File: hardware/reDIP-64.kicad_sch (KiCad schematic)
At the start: 0 parts

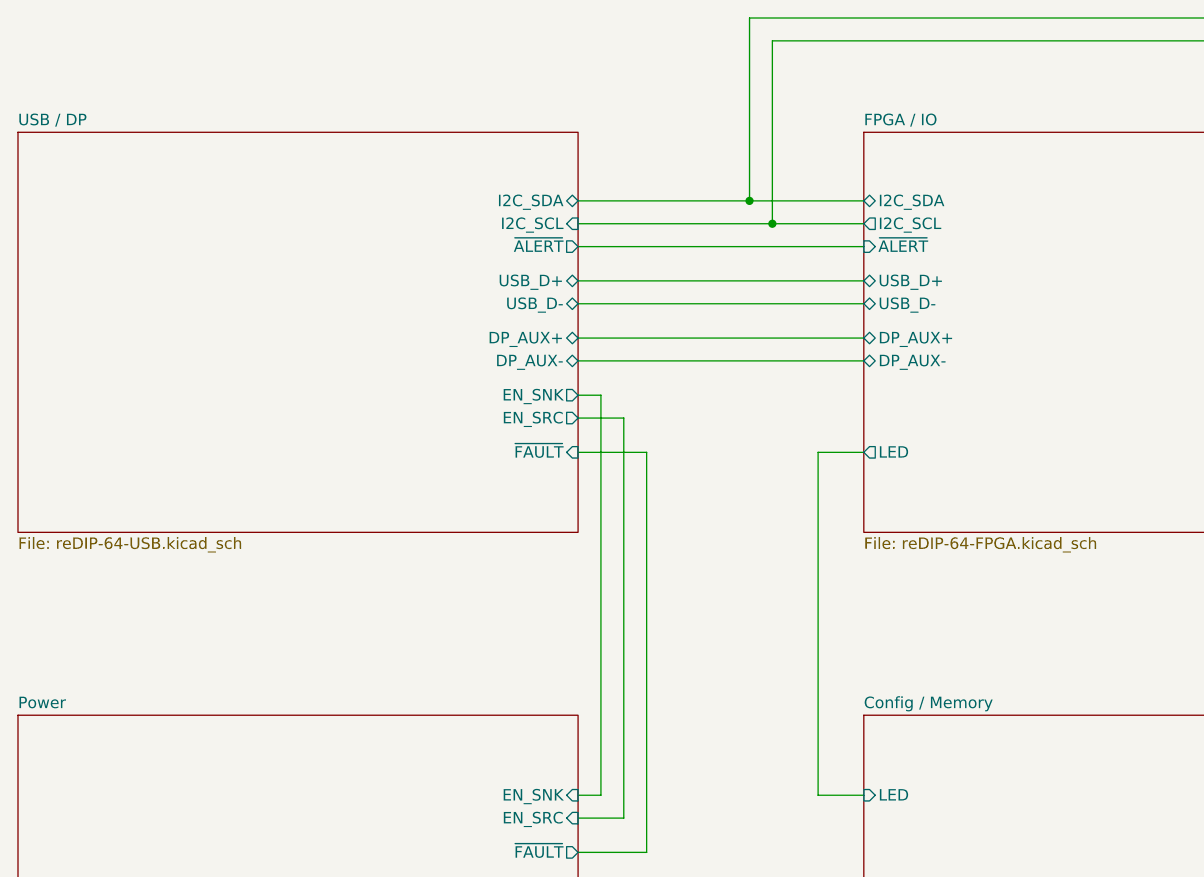
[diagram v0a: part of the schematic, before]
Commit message: Various improvements
* Removed slash from sheet names
* Reannotated schematics
* Example derivation of clocks in schematics
* Identical capacitors for DisplayPort main lanes and AUX
* Replaced switch FSA2259UMX with FSUSB42UMX
* Modified PCB physical stackup to (hopefully) be manufacturable
* Only one microvia size (0.1mm)
* Changed track width for differential pairs
* Routing cleanups and improvements
* Added files for manufacture
* Updated README

Many thanks for advice and help go to @azonenberg, @DX-MON, @gatecat,
@smunaut, and @zyp.
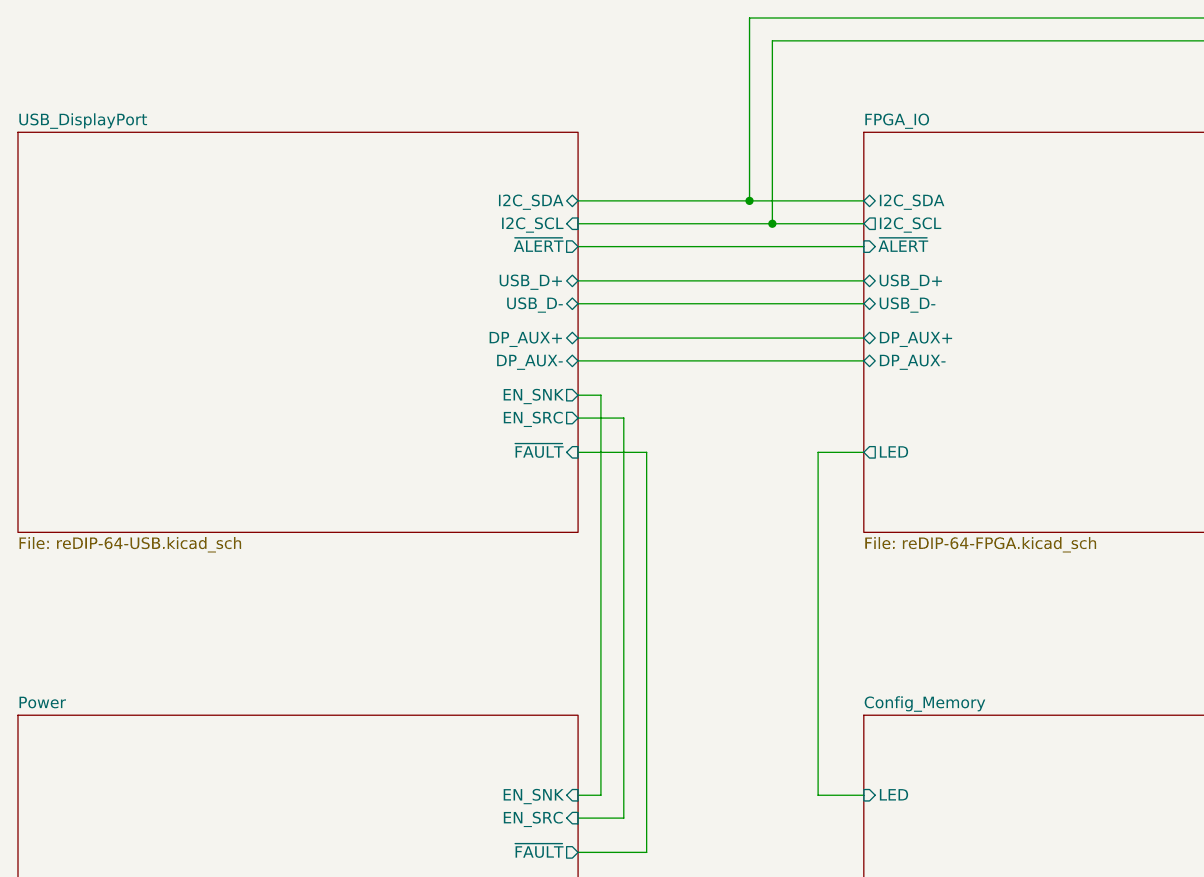
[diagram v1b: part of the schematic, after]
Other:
- sheet Config / Memory renamed Config_Memory
- sheet FPGA / IO renamed FPGA_IO
- sheet USB / DP renamed USB_DisplayPort

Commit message: Updated all KiCad files to current format
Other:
- sheet FPGA_IO ports: added ~{ALERT}; removed ~ALERT~
- sheet Power ports: added ~{FAULT}; removed ~FAULT~
- sheet USB_DisplayPort ports: added ~{ALERT}, ~{FAULT}; removed ~ALERT~, ~FAULT~

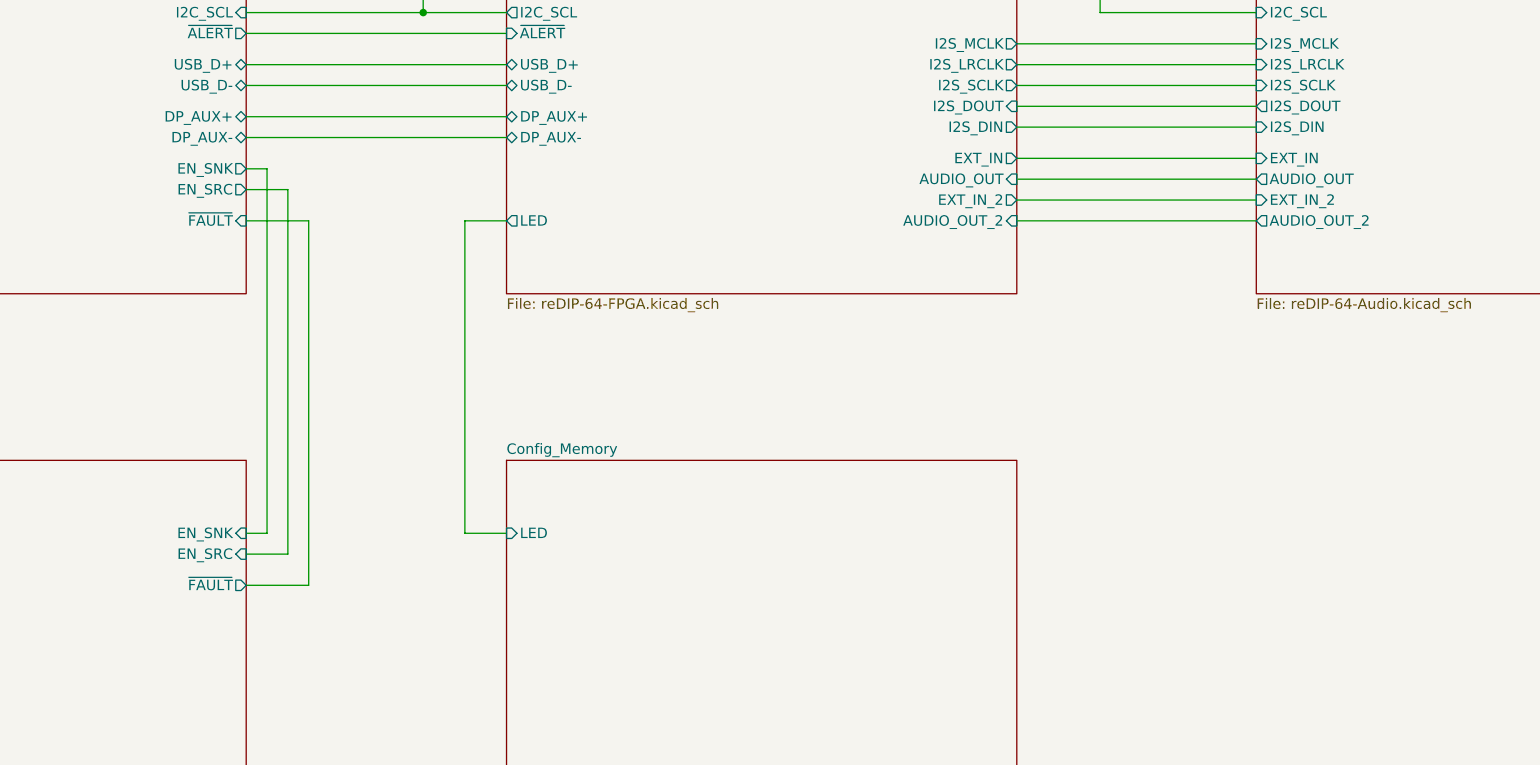
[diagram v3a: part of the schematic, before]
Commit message: Revision 1.0
* USB receptacle replaced with GCT USB4080-03-A / HRO TYPE-C-31-M-05
* USB PD TCPC changed to PTN5110NHQ (FPF2286 has 15ms VBUS debounce time)
* Complete rework of power section
  - Over-voltage protection on VBUS (FPF2286 / FPF2495C)
  - Bidirectional VCC (2 x TPS22916)
  - Replaced EOLed buck converters with FAN53610 / FAN53611
  - Replaced EOLed LDO for ECP5 VCCAUX with NCP115AMX250TCG
  - Replaced LDO for SGTL5000 VDDA with 3.3V version
  - Added separate LDO for SGTL5000 VDDD, avoiding overvoltage on ECP5 VCC
* Bus switch changed to SN74CBT16211A, biased for level shifting
* Registered I/O for FLASH / HyperRAM clock
* Pin header changes:
  - Machined (round) pins for MOS6510 socket
  - Top only headers for additional I/O
  - Reworked pinout for VIC-II and SID
  - Removed 5V output (now available on bidirectional VCC)
  - Added GND for audio / 3.3V
  - Changed JTAG pinout to match Tag-Connect TC-LATTICE / TC-XILINX6
* Removed EXT_IN capacitors
* Button force changed from 240gf to 100gf
* Space for UL and date codes
* Black solder mask
* Silk screen updates
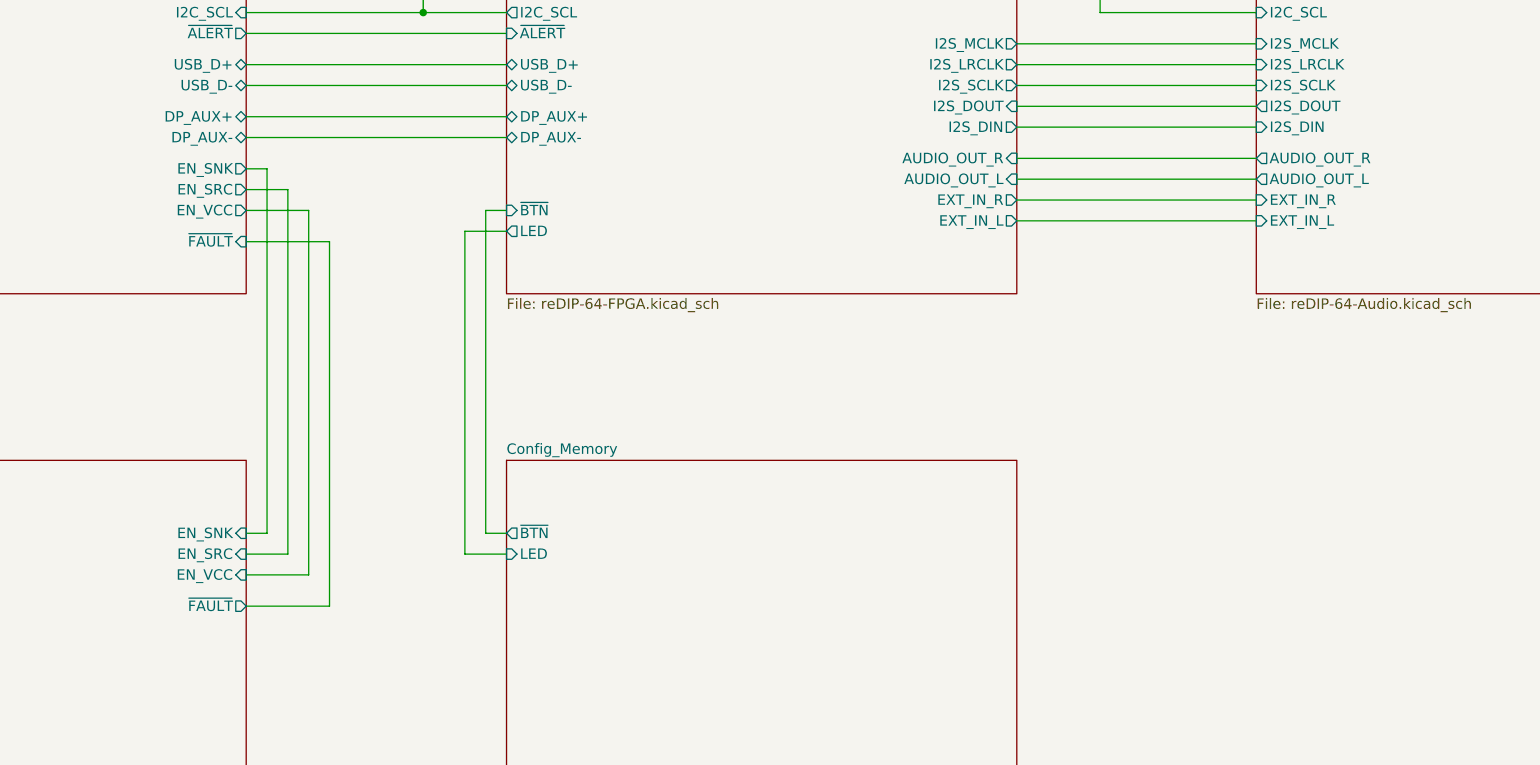
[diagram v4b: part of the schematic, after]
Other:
- sheet Audio ports: added AUDIO_OUT_L, AUDIO_OUT_R, EXT_IN_L, EXT_IN_R; removed AUDIO_OUT, AUDIO_OUT_2, EXT_IN, EXT_IN_2
- sheet Config_Memory ports: added ~{BTN}; removed none
- sheet FPGA_IO ports: added AUDIO_OUT_L, AUDIO_OUT_R, EXT_IN_L, EXT_IN_R, ~{BTN}; removed AUDIO_OUT, AUDIO_OUT_2, EXT_IN, EXT_IN_2
- sheet Power ports: added EN_VCC; removed none
- sheet USB_DisplayPort ports: added EN_VCC; removed none
